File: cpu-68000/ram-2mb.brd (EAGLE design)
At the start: 160 x 100 mm, 72 parts, among them IC101 74HC245DW, IC102 74HC245DW, IC103 74HC245DW, IC104 74HC245DW, IC105 74HC243D, IC106 74HC138D, IC107 GAL22V10D

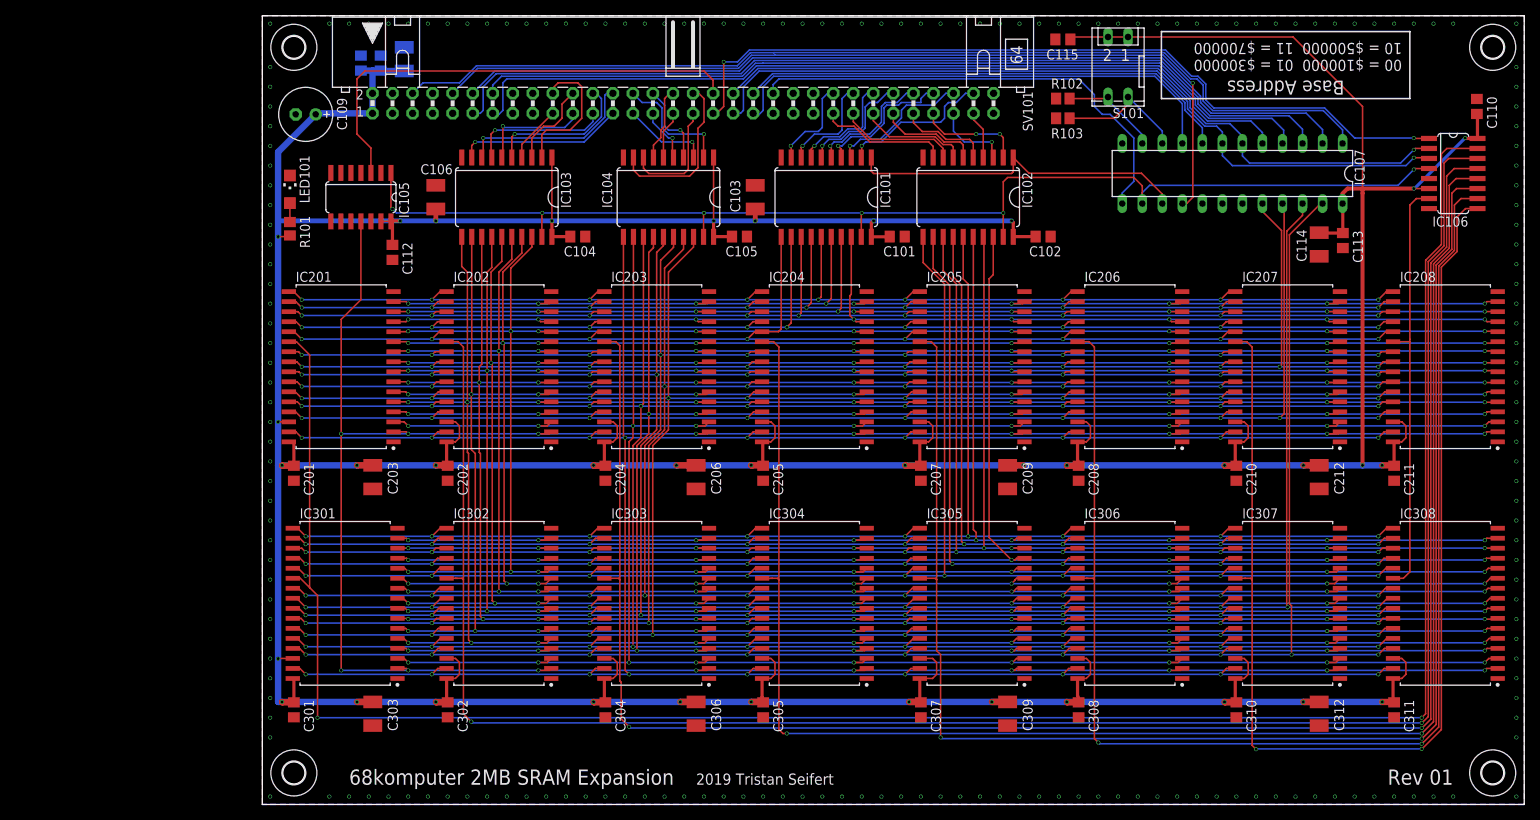
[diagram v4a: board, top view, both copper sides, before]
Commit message: Rev01 of CPU-68000 and 2MB SRAM board sent to production
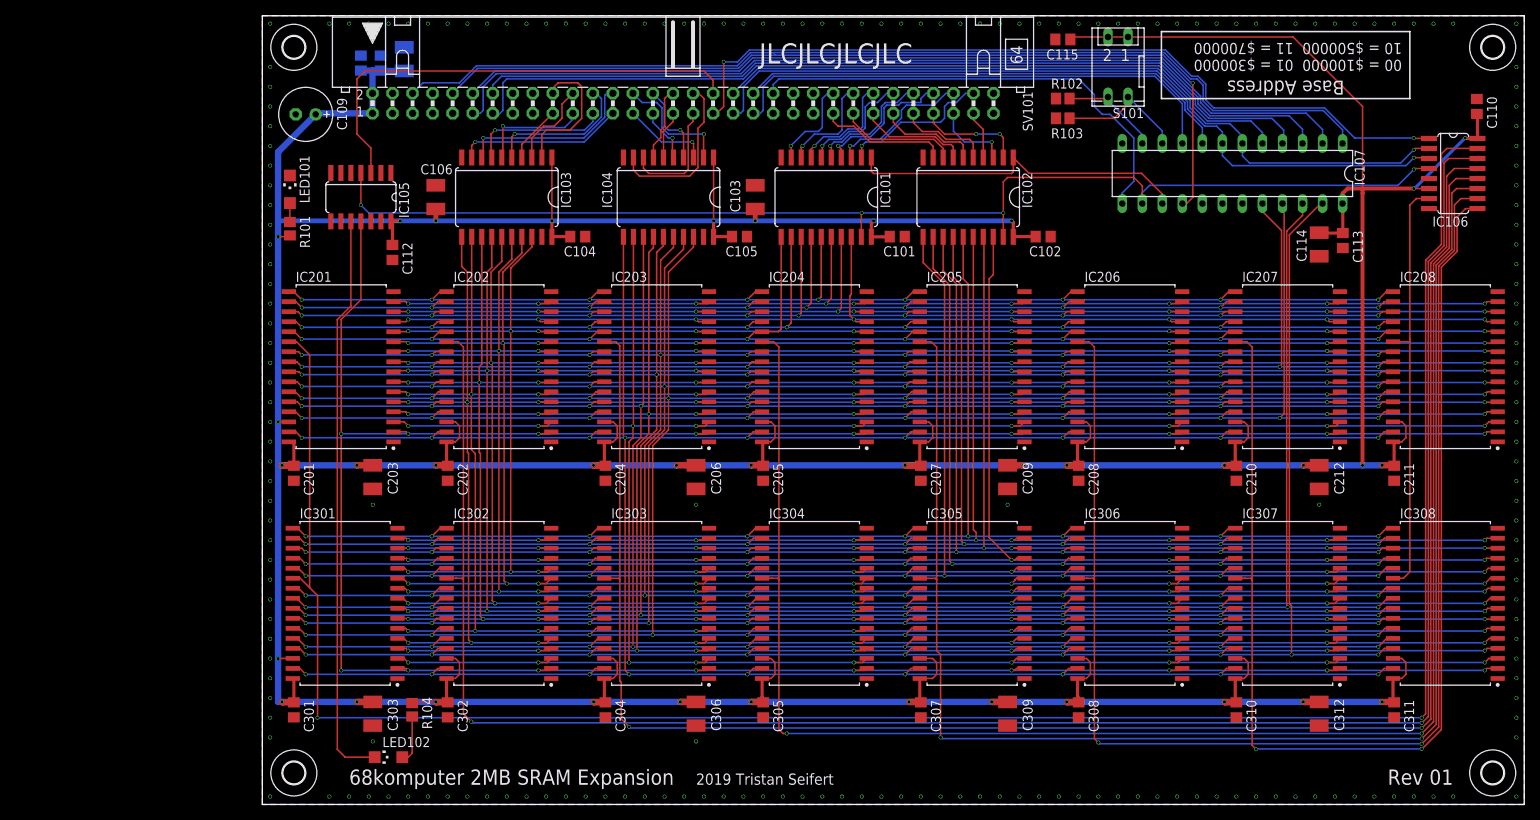
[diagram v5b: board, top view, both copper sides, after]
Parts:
- added LED102: (no value), led:CHIPLED_1206
- added R104: 3k, rcl:R2012
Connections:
- removed net N$5: IC107.19
- removed net N$6: IC107.18
- removed net N$7: IC107.17
- new net !CS_LED: IC105.10, LED102.C
- new net N$1: LED102.A, R104.2
- net !CS: now also IC105.4; no longer IC103.19, IC104.19, IC105.1
- net +5V: now also R104.1; no longer IC105.13
- net GND: now also IC103.19, IC104.19, IC105.1, IC105.13; no longer IC105.4
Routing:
- net !CS_LED: track 0.00 -> 72.8 mm
- net N$1: track 0.00 -> 6.11 mm
- net !CS: track 158.0 -> 155.5 mm, vias 6 -> 4
- net +5V: track 803.5 -> 804.2 mm
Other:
- board text added: "JLCJLCJLCJLC"
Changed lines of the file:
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@@
 10 = $500000  11 = $700000</text>
 <text x="151" y="2.5" size="1.9304" layer="25" align="bottom-right">Rev 01</text>
+<text x="63" y="96.5" size="2.54" layer="25" align="top-left">JLCJLCJLCJLC</text>
 </plain>
 <attributes>
@@
 <attribute name="SPICEPREFIX" value="C" x="16.5" y="70" size="1.4224" layer="27" rot="R270" display="off"/>
 </element>
+<element name="R104" library="rcl" library_urn="urn:adsk.eagle:library:334" package="R2012" package3d_urn="urn:adsk.eagle:package:23543/2" value="3k" x="19" y="12" smashed="yes" rot="R270">
+<attribute name="MOUSER" value="652-CR0805JW-302ELF" x="19" y="12" size="2.54" layer="27" rot="R270" display="off"/>
+<attribute name="NAME" x="20.27" y="13.635" size="1.27" layer="25" rot="R270"/>
+<attribute name="SPICEPREFIX" value="R" x="19" y="12" size="2.54" layer="27" rot="R270" display="off"/>
+</element>
+<element name="LED102" library="led" library_urn="urn:adsk.eagle:library:259" package="CHIPLED_1206" package3d_urn="urn:adsk.eagle:package:15823/2" value="" x="16" y="6" smashed="yes" rot="R90">
+<attribute name="MOUSER" value="710-156120VS75300" x="9.5" y="-1" size="2.54" layer="27" rot="R90" display="off"/>
+<attribute name="NAME" x="15.23" y="7.27" size="1.27" layer="25"/>
+<attribute name="VALUE" x="17.27" y="8.54" size="1.27" layer="27" rot="R180"/>
+</element>
 </elements>
 <signals>
@@
 <contactref element="C312" pad="+"/>
 <contactref element="C311" pad="1"/>
-<wire x1="23.45" y1="43" x2="23.5" y2="42.95" width="0.8128" layer="1"/>
-<wire x1="54.95" y1="42.95" x2="55" y2="43" width="0.8128" layer="1"/>
-<wire x1="94.45" y1="42.95" x2="94.5" y2="43" width="0.8128" layer="1"/>
 <wire x1="103.45" y1="43" x2="103.665634375" y2="43" width="0.8128" layer="1"/>
 <wire x1="103.45" y1="43" x2="103.5" y2="42.95" width="0.8128" layer="1"/>
 <wire x1="123.5" y1="42.95" x2="123.55" y2="43" width="0.8128" layer="1"/>
 <wire x1="123.55" y1="43" x2="123.62113125" y2="43" width="0.8128" layer="1"/>
-<wire x1="134.05" y1="12.95" x2="134" y2="13" width="0.8128" layer="1"/>
-<wire x1="123.55" y1="13" x2="123.5" y2="12.95" width="0.8128" layer="1"/>
-<wire x1="94.55" y1="12.95" x2="94.5" y2="13" width="0.8128" layer="1"/>
-<wire x1="94.5" y1="13" x2="94.45" y2="12.95" width="0.8128" layer="1"/>
-<wire x1="55.05" y1="12.95" x2="55" y2="13" width="0.8128" layer="1"/>
-<wire x1="43.55" y1="13" x2="43.5" y2="12.95" width="0.8128" layer="1"/>
-<wire x1="14.05" y1="12.95" x2="14" y2="13" width="0.8128" layer="1"/>
-<wire x1="14" y1="13" x2="13.95" y2="12.95" width="0.8128" layer="1"/>
 <wire x1="143.3639" y1="15.975" x2="143.3639" y2="13.0861" width="0.4064" layer="1"/>
 <wire x1="143.5" y1="12.95" x2="143.3639" y2="13.0861" width="0.4064" layer="1"/>
@@
 <wire x1="23.3639" y1="15.975" x2="23.3639" y2="13.0861" width="0.4064" layer="1"/>
 <wire x1="23.5" y1="12.95" x2="23.3639" y2="13.0861" width="0.4064" layer="1"/>
-<wire x1="4.1" y1="13.05" x2="4" y2="12.95" width="0.4064" layer="1"/>
 <wire x1="4" y1="42.95" x2="4" y2="45.919009375" width="0.4064" layer="1"/>
 <wire x1="4" y1="45.919009375" x2="3.3639" y2="45.975" width="0.4064" layer="1"/>
@@
 <wire x1="2" y1="18.5" x2="2" y2="43" width="0.8128" layer="16"/>
 <wire x1="2" y1="43" x2="2" y2="48.5" width="0.8128" layer="16"/>
-<wire x1="3.95" y1="43" x2="4" y2="42.95" width="0.8128" layer="1"/>
 <wire x1="2" y1="74" x2="2" y2="72" width="0.8128" layer="16"/>
 <wire x1="2" y1="72" x2="2" y2="48.5" width="0.8128" layer="16"/>
@@
 <wire x1="94.5" y1="43" x2="96.5" y2="43" width="0.8128" layer="1"/>
 <via x="96.5" y="43" extent="1-16" drill="0.35"/>
-<wire x1="62.05" y1="42.95" x2="62" y2="43" width="0.8128" layer="1"/>
 <via x="62" y="43" extent="1-16" drill="0.35"/>
 <wire x1="55" y1="43" x2="52.5" y2="43" width="0.8128" layer="1"/>
@@
 <contactref element="C112" pad="1"/>
 <contactref element="IC105" pad="14"/>
-<contactref element="IC105" pad="13"/>
-<wire x1="15.04" y1="73.9266" x2="16.31" y2="73.9266" width="0.2032" layer="1"/>
 <wire x1="16.31" y1="73.9266" x2="16.3834" y2="74" width="0.2032" layer="1"/>
 <wire x1="16.3834" y1="74" x2="17.5" y2="74" width="0.4064" layer="1"/>
@@
 <wire x1="63.3639" y1="45.975" x2="63.45" y2="45.8889" width="0.4064" layer="1"/>
 <wire x1="63.45" y1="45.8889" x2="63.45" y2="43" width="0.4064" layer="1"/>
+<contactref element="R104" pad="1"/>
+<wire x1="19.15" y1="13" x2="19" y2="12.85" width="0.2032" layer="1"/>
+<wire x1="22" y1="13" x2="19.15" y2="13" width="0.2032" layer="1"/>
 </signal>
 <signal name="GND">
@@
 <contactref element="IC105" pad="7"/>
 <contactref element="IC105" pad="6"/>
-<contactref element="IC105" pad="4"/>
 <contactref element="IC105" pad="5"/>
 <contactref element="C110" pad="2"/>
 <contactref element="C112" pad="2"/>
+<contactref element="IC104" pad="19"/>
+<contactref element="IC103" pad="19"/>
+<contactref element="IC105" pad="13"/>
+<contactref element="IC105" pad="1"/>
+<via x="14" y="8" extent="1-16" drill="0.35"/>
 </signal>
 <signal name="D0">
@@
 <contactref element="IC101" pad="19"/>
 <contactref element="IC102" pad="19"/>
-<contactref element="IC103" pad="19"/>
-<contactref element="IC104" pad="19"/>
 <contactref element="IC107" pad="14"/>
 <wire x1="111.57" y1="76.19" x2="111.57" y2="77.57" width="0.2032" layer="16"/>
@@
 <wire x1="111.57" y1="78.43" x2="111.57" y2="76.19" width="0.2032" layer="1"/>
 <wire x1="110.5" y1="79.5" x2="111.57" y2="78.43" width="0.2032" layer="1"/>
-<wire x1="35.445" y1="71.9708" x2="35.445" y2="74.945" width="0.2032" layer="1"/>
-<wire x1="35.445" y1="74.945" x2="35.5" y2="75" width="0.2032" layer="1"/>
-<via x="35.5" y="75" extent="1-16" drill="0.35"/>
-<wire x1="35.5" y1="75" x2="56" y2="75" width="0.2032" layer="16"/>
 <via x="93.945" y="75" extent="1-16" drill="0.35"/>
-<wire x1="56" y1="75" x2="76" y2="75" width="0.2032" layer="16"/>
 <wire x1="76" y1="75" x2="93.945" y2="75" width="0.2032" layer="16"/>
 <wire x1="75.945" y1="71.9708" x2="75.945" y2="74.945" width="0.2032" layer="1"/>
 <wire x1="75.945" y1="74.945" x2="76" y2="75" width="0.2032" layer="1"/>
 <via x="76" y="75" extent="1-16" drill="0.35"/>
-<wire x1="55.945" y1="71.9708" x2="55.945" y2="74.945" width="0.2032" layer="1"/>
-<wire x1="55.945" y1="74.945" x2="56" y2="75" width="0.2032" layer="1"/>
-<via x="56" y="75" extent="1-16" drill="0.35"/>
-<contactref element="IC105" pad="1"/>
-<wire x1="35.5" y1="75" x2="17" y2="75" width="0.2032" layer="16"/>
-<wire x1="17" y1="75" x2="16.5" y2="75.5" width="0.2032" layer="16"/>
-<via x="16.5" y="75.5" extent="1-16" drill="0.35"/>
-<wire x1="16.5" y1="75.5" x2="16.31" y2="75.69" width="0.2032" layer="1"/>
-<wire x1="16.31" y1="75.69" x2="16.31" y2="80.0734" width="0.2032" layer="1"/>
+<contactref element="IC105" pad="4"/>
+<wire x1="76" y1="75" x2="13.5" y2="75" width="0.2032" layer="16"/>
+<wire x1="13.5" y1="75" x2="12.5" y2="76" width="0.2032" layer="16"/>
+<via x="12.5" y="76" extent="1-16" drill="0.35"/>
+<wire x1="12.5" y1="76" x2="12.5" y2="80.0734" width="0.2032" layer="1"/>
 </signal>
 <signal name="!RD">
@@
 <wire x1="107.04" y1="89.5" x2="107.23" y2="89.69" width="0.2032" layer="1"/>
 </signal>
-<signal name="N$5">
-<contactref element="IC107" pad="19"/>
-</signal>
-<signal name="N$6">
-<contactref element="IC107" pad="18"/>
-</signal>
-<signal name="N$7">
-<contactref element="IC107" pad="17"/>
-</signal>
 <signal name="N$18">
 <contactref element="R101" pad="2"/>
@@
 <contactref element="SV101" pad="41"/>
 </signal>
+<signal name="GND1">
+<via x="55" y="8" extent="1-16" drill="0.35"/>
+</signal>
+<signal name="GND2">
+<via x="14" y="38" extent="1-16" drill="0.35"/>
+</signal>
+<signal name="GND3">
+<via x="55" y="38" extent="1-16" drill="0.35"/>
+</signal>
+<signal name="GND4">
+<via x="94.5" y="38" extent="1-16" drill="0.35"/>
+</signal>
+<signal name="GND5">
+<via x="134" y="38" extent="1-16" drill="0.35"/>
+</signal>
+<signal name="!CS_LED">
+<contactref element="IC105" pad="10"/>
+<wire x1="11.23" y1="73.9266" x2="11.23" y2="63.196975" width="0.2032" layer="1"/>
+<wire x1="9.5" y1="7" x2="10.5" y2="6" width="0.2032" layer="1"/>
+<wire x1="11.23" y1="63.196975" x2="9.5" y2="61.466975" width="0.2032" layer="1"/>
+<wire x1="9.5" y1="61.466975" x2="9.5" y2="7" width="0.2032" layer="1"/>
+<contactref element="LED102" pad="C"/>
+<wire x1="10.5" y1="6" x2="14.25" y2="6" width="0.2032" layer="1"/>
+</signal>
+<signal name="N$1">
+<contactref element="R104" pad="2"/>
+<contactref element="LED102" pad="A"/>
+<wire x1="19" y1="11.15" x2="19" y2="6.5" width="0.2032" layer="1"/>
+<wire x1="19" y1="6.5" x2="18.5" y2="6" width="0.2032" layer="1"/>
+<wire x1="18.5" y1="6" x2="17.75" y2="6" width="0.2032" layer="1"/>
+</signal>
 </signals>
